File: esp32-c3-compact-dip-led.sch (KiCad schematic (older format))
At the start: 29 parts, among them J1 PJ-102A compatible 5.5/2.1mm, J2 USB-C POWER ONLY, J3 LED OUT, J4 M5STACK A105, Q1 RJP020N06T100, U1 ESP32-C3-WROOM-02-N4, U2 LMR36510FADDAR

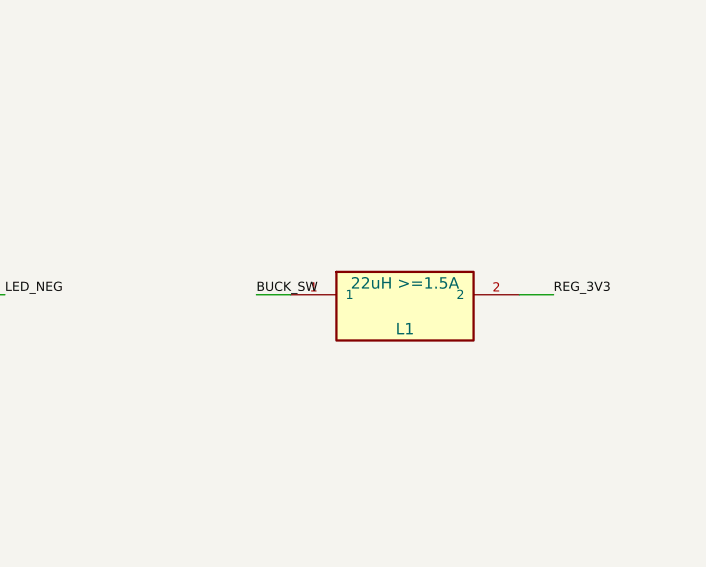
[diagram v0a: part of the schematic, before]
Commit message: Use lower-cost 2A buck inductor
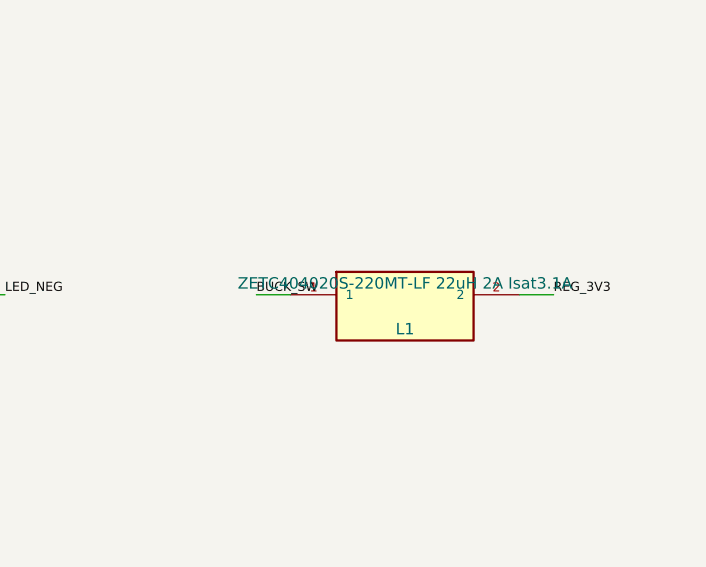
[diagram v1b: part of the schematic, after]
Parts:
- L1: value 22uH >=1.5A -> ZETC404020S-220MT-LF 22uH 2A Isat3.1A
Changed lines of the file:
@@
 P 13000 3100
 F 0 "L1" H 13000 3000 50  0000 C CNN
-F 1 "22uH >=1.5A" H 13000 3200 50  0000 C CNN
+F 1 "ZETC404020S-220MT-LF 22uH 2A Isat3.1A" H 13000 3200 50  0000 C CNN
 	1    13000 3100
 	1 0 0 -1
